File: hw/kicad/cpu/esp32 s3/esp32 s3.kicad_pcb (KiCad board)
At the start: 2 copper layers, 45 x 45 mm, 40 parts, among them J1 TOP, J2 BUTTOM, J3 USB_B_Micro, SW1 SW_Push, U1 ESP32-S3-WROOM-1-N16R2, U2 ICM-42688-P

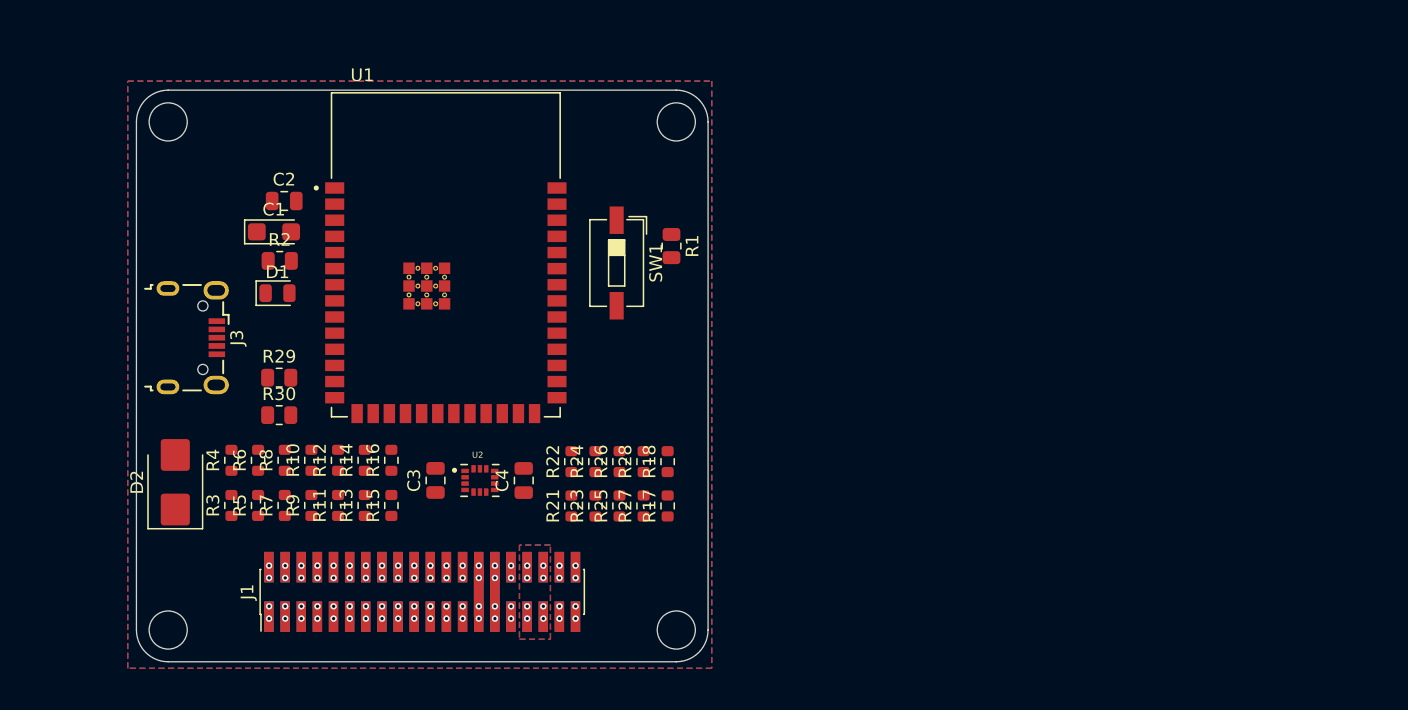
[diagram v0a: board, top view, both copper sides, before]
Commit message: 尽力改成40mmx40mm
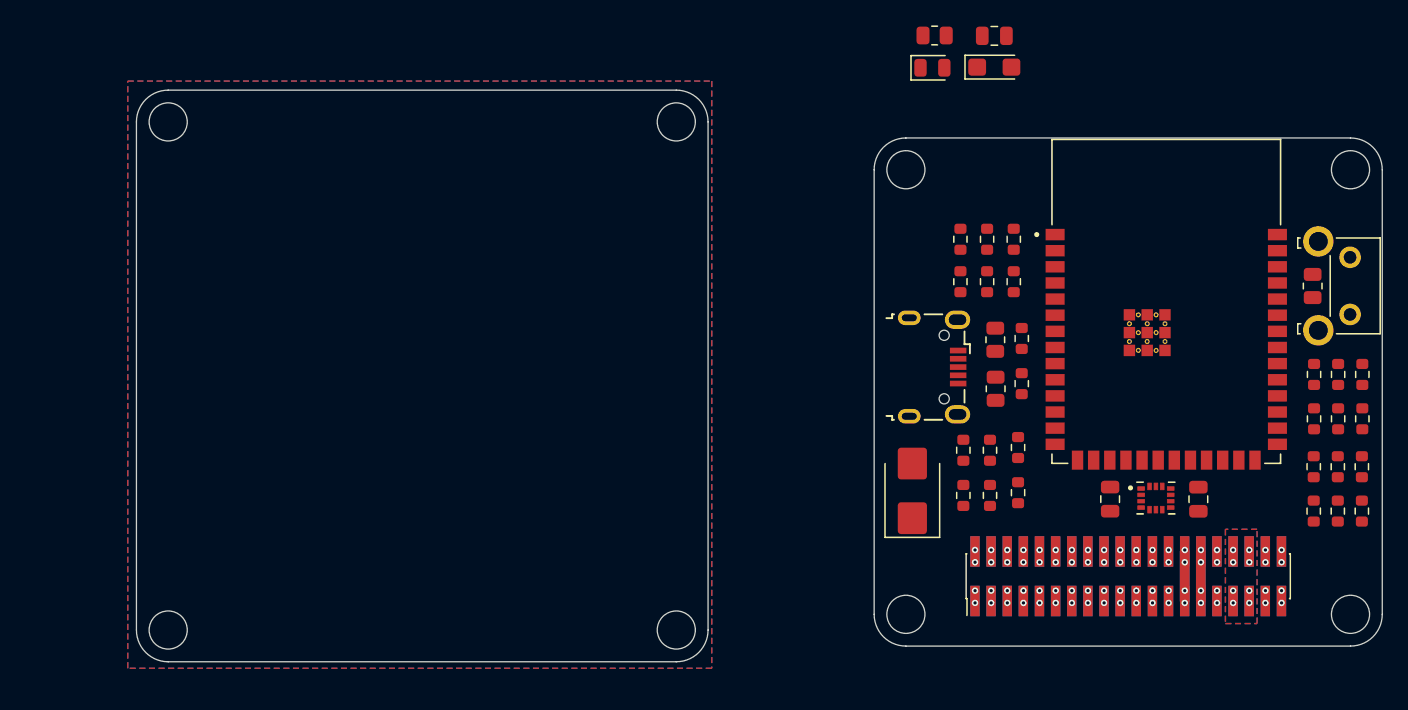
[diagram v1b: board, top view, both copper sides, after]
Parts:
- added R20: 100, Resistor_SMD:R_0603_1608Metric, F.Cu at (147.2, 58.6)
- added R31: 100, Resistor_SMD:R_0603_1608Metric, F.Cu at (147.2, 55.1)
- SW1: footprint Button_Switch_SMD:SW_DIP_SPSTx01_Slide_6.7x4.1mm_W6.73mm_P2.54mm_LowProfile_JPin -> Button_Switch_THT:SW_SPST_Omron_B3F-315x_Angled
- moved R3 60.0 mm to (115.6, 47.8)
- moved R5 60.0 mm to (117.7, 47.8)
- moved R7 60.0 mm to (119.8, 47.8)
- moved R4 60.0 mm to (115.6, 44.5)
- moved R6 60.0 mm to (117.7, 44.5)
- moved R8 60.0 mm to (119.8, 44.5)
- moved R25 58.4 mm to (147.2, 65.9)
- moved R21 58.4 mm to (143.4, 65.9)
- moved R23 58.4 mm to (145.3, 65.9)
- moved R26 58.4 mm to (147.2, 62.4)
- moved R22 58.4 mm to (143.4, 62.4)
- moved R24 58.4 mm to (145.3, 62.4)
- moved J3 58.4 mm to (113.5, 54.5)
- moved C1 58.2 mm to (118.3, 30.9)
- moved D2 58.0 mm to (111.8, 64.3)
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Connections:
- J1 pad 10: /UART3_Tx -> /I2C_CLK
- J1 pad 11: /I2C_SDA -> /SPI_CS
- J1 pad 12: /I2C_CLK -> /SPI_CLK
- J1 pad 13: /SPI_CS -> /SPI_MOSI
- J1 pad 14: /SPI_CLK -> /SPI_MISO
- J1 pad 15: /SPI_MOSI -> /GPIO_1
- J1 pad 16: /SPI_MISO -> /GPIO_2
- J1 pad 17: /GPIO_1 -> /GPIO_3
- J1 pad 18: /GPIO_2 -> /GPIO_4
- J1 pad 19: /GPIO_3 -> /GPIO_5
- J1 pad 20: /GPIO_4 -> /GPIO_6
- J1 pad 21: /GPIO_5 -> /GPIO_7
- J1 pad 22: /GPIO_6 -> /GPIO_8
- J1 pad 23: /GPIO_7 -> /GPIO_9
- J1 pad 24: /GPIO_8 -> /GPIO_10
- J1 pad 25: /GPIO_9 -> /GPIO_11
- J1 pad 26: /GPIO_10 -> /GPIO_12
- J1 pad 9: /UART3_Rx -> /I2C_SDA
- J2 pad 10: /UART3_Rx -> /I2C_SDA
- J2 pad 11: /I2C_CLK -> /SPI_CLK
- J2 pad 12: /I2C_SDA -> /SPI_CS
- J2 pad 13: /SPI_CLK -> /SPI_MISO
- J2 pad 14: /SPI_CS -> /SPI_MOSI
- J2 pad 15: /SPI_MISO -> /GPIO_2
- J2 pad 16: /SPI_MOSI -> /GPIO_1
- J2 pad 17: /GPIO_2 -> /GPIO_4
- J2 pad 18: /GPIO_1 -> /GPIO_3
- J2 pad 19: /GPIO_4 -> /GPIO_6
- J2 pad 20: /GPIO_3 -> /GPIO_5
- J2 pad 21: /GPIO_6 -> /GPIO_8
- J2 pad 22: /GPIO_5 -> /GPIO_7
- J2 pad 23: /GPIO_8 -> /GPIO_10
- J2 pad 24: /GPIO_7 -> /GPIO_9
- J2 pad 25: /GPIO_10 -> /GPIO_12
- J2 pad 26: /GPIO_9 -> /GPIO_11
- J2 pad 9: /UART3_Tx -> /I2C_CLK
- R10 pad 2: /UART2_TX -> /UART2_Tx
- R11 pad 1: /i2c_clk -> /i2c_sda
- R12 pad 1: /i2c_sda -> /i2c_clk
- R13 pad 1: /spi3_cs -> /spi2_cs
- R14 pad 1: /spi3_clk -> /spi2_clk
- R15 pad 1: /spi3_mosi -> /spi2_mosi
- R16 pad 1: /spi3_miso -> /spi2_miso
- R26 pad 1: /gpio5 -> /gpio6
- R29 pad 2: /USB+ -> /usb+
- R30 pad 2: /USB- -> /usb-
- R7 pad 2: /UART1_RX -> /UART1_Rx
- R8 pad 2: /UART1_TX -> /UART1_Tx
- R9 pad 2: /UART2_RX -> /UART2_Rx
- U1 pad 10: /i2c_clk -> /i2c_sda
- U1 pad 11: /i2c_sda -> /i2c_clk
- U1 pad 13: /usb_d- -> /usb-
- U1 pad 14: /usb_d+ -> /usb+
- U1 pad 15: unconnected-(U1-IO3-Pad15) -> /spi2_miso
- U1 pad 16: unconnected-(U1-IO46-Pad16) -> /spi2_cs
- U1 pad 17: /spi2_cs -> /spi2_mosi
- U1 pad 18: /spi2_mosi -> /spi2_clk
- U1 pad 19: /spi2_clk -> /spi3_miso
- U1 pad 20: /spi2_miso -> /IMU_FSYNC
- U1 pad 24: /spi3_miso -> /gpio1
- U1 pad 25: /IMU_FSYNC -> /gpio2
- U1 pad 26: unconnected-(U1-IO45-Pad26) -> Net-(U1-IO45)
- U1 pad 28: /gpio1 -> /gpio3
- U1 pad 29: /gpio2 -> /gpio4
- U1 pad 30: /gpio3 -> /gpio5
- U1 pad 31: /gpio4 -> /gpio6
- U1 pad 32: /gpio5 -> /gpio7
- U1 pad 33: /gpio5 -> /gpio8
- U1 pad 34: /gpio7 -> /gpio9
- U1 pad 35: /gpio8 -> /gpio10
- U1 pad 38: /gpio9 -> /gpio11
- U1 pad 39: /gpio10 -> /gpio12
- U1 pad 8: /uart1_tx -> /uart1_rx
- U1 pad 9: /uart1_rx -> /uart1_tx
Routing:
- net /UART3_Tx: vias 2 -> 0
- net /UART3_Rx: vias 2 -> 0
- net /GPIO_12: vias 0 -> 2
- net /GPIO_11: vias 0 -> 2
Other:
- board size 45 x 45 mm -> 98.1 x 45 mm

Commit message: esp32部分该小板框可太难了，小电阻太多，只好全部去掉。
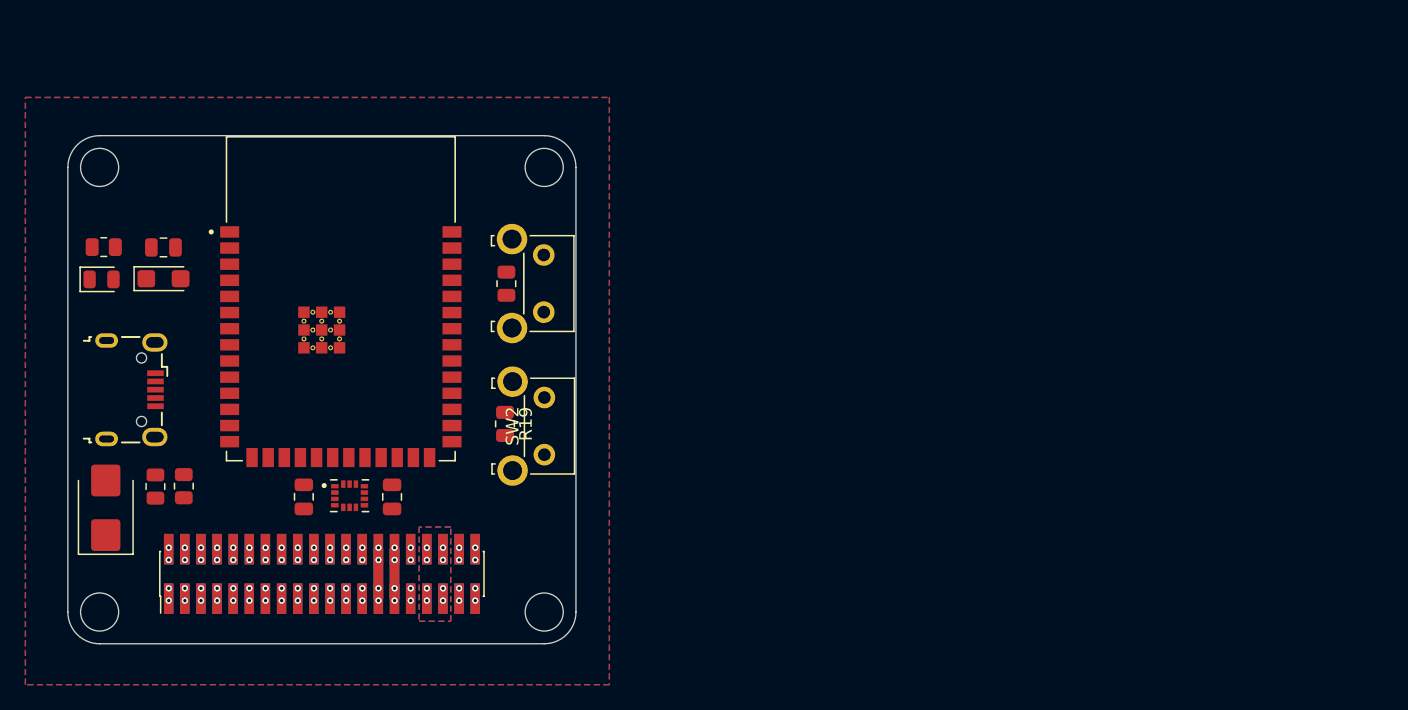
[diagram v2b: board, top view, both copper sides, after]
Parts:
- removed R10, R11, R12, R13, R14, R15, R16, R17, R18, R20, R21, R22, R23, R24, R25, R26, R27, R28, R3, R31, R4, R5, R6, R7, R8, R9: 100, Resistor_SMD:R_0603_1608Metric
- added R19: 1k, Resistor_SMD:R_0805_2012Metric, F.Cu at (79.7, 59.0)
- added SW2: SW_Push, Button_Switch_THT:SW_SPST_Omron_B3F-315x_Angled, F.Cu at (82.8, 56.9)
- moved C1 67.5 mm to (52.8, 47.6)
- moved C2 67.5 mm to (52.8, 45.1)
- moved D1 67.5 mm to (48.0, 47.6)
- moved R2 67.5 mm to (48.1, 45.1)
- moved R30 67.1 mm to (52.2, 63.9)
- moved U1 65.0 mm to (66.8, 49.1)
- moved R29 64.4 mm to (54.5, 63.9)
- moved D2 63.5 mm to (48.3, 65.6)
- moved R1 63.5 mm to (79.8, 48.0)
- moved U2 63.5 mm to (67.5, 64.6)
- moved C3 63.5 mm to (63.9, 64.7)
- moved C4 63.5 mm to (70.8, 64.7)
- moved SW1 63.5 mm to (82.8, 45.7)
- moved J1 63.5 mm to (65.3, 70.8)
- moved J2 63.5 mm to (65.3, 70.8)
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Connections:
- U1 pad 10: /i2c_sda -> /I2C_SDA
- U1 pad 11: /i2c_clk -> /I2C_CLK
- U1 pad 15: /spi2_miso -> /SPI_MISO
- U1 pad 16: /spi2_cs -> /SPI_CS
- U1 pad 17: /spi2_mosi -> /SPI_MOSI
- U1 pad 18: /spi2_clk -> /SPI_CLK
- U1 pad 24: /gpio1 -> /GPIO_1
- U1 pad 25: /gpio2 -> /GPIO_2
- U1 pad 28: /gpio3 -> /GPIO_3
- U1 pad 29: /gpio4 -> /GPIO_4
- U1 pad 30: /gpio5 -> /GPIO_5
- U1 pad 31: /gpio6 -> /GPIO_6
- U1 pad 32: /gpio7 -> /GPIO_7
- U1 pad 33: /gpio8 -> /GPIO_8
- U1 pad 34: /gpio9 -> /GPIO_9
- U1 pad 35: /gpio10 -> /GPIO_10
- U1 pad 36: /uart0_rx -> /UART1_Rx
- U1 pad 37: /uart0_tx -> /UART1_Tx
- U1 pad 38: /gpio11 -> /GPIO_11
- U1 pad 39: /gpio12 -> /GPIO_12
- U1 pad 4: /adc1_ch3 -> /ADC_1
- U1 pad 5: /adc1_ch4 -> /ADC_2
- U1 pad 6: /adc1_ch5 -> /ADC_3
- U1 pad 7: /adc1_ch6 -> /ADC_4
- U1 pad 8: /uart1_rx -> /UART2_Rx
- U1 pad 9: /uart1_tx -> /UART2_Tx
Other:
- board size 98.1 x 45 mm -> 40 x 40 mm

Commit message: Merge from normal
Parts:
- removed SW2: SW_Push, Button_Switch_THT:SW_SPST_Omron_B3F-315x_Angled
- added R10: R, Resistor_SMD:R_0603_1608Metric, F.Cu at (65.4, 52.3)
- added R11: R, Resistor_SMD:R_0603_1608Metric, F.Cu at (65.4, 53.8)
- added R12: R, Resistor_SMD:R_0603_1608Metric, F.Cu at (65.4, 55.3)
- added R13: R, Resistor_SMD:R_0603_1608Metric, F.Cu at (65.4, 56.8)
- added R14: R, Resistor_SMD:R_0603_1608Metric, F.Cu at (65.4, 58.3)
- added R15: R, Resistor_SMD:R_0603_1608Metric, F.Cu at (65.4, 59.8)
- added R16: R, Resistor_SMD:R_0603_1608Metric, F.Cu at (65.4, 61.3)
- added R17: R, Resistor_SMD:R_0603_1608Metric, F.Cu at (90.2, 58.4)
- added R18: R, Resistor_SMD:R_0603_1608Metric, F.Cu at (90.2, 56.9)
- added R20: R, Resistor_SMD:R_0603_1608Metric, F.Cu at (90.2, 53.8)
- added R21: R, Resistor_SMD:R_0603_1608Metric, F.Cu at (90.2, 52.3)
- added R22: R, Resistor_SMD:R_0603_1608Metric, F.Cu at (90.2, 50.8)
- added R23: R, Resistor_SMD:R_0603_1608Metric, F.Cu at (90.2, 49.3)
- added R24: R, Resistor_SMD:R_0603_1608Metric, F.Cu at (90.2, 47.8)
- added R25: R, Resistor_SMD:R_0603_1608Metric, F.Cu at (90.2, 46.3)
- added R26: R, Resistor_SMD:R_0603_1608Metric, F.Cu at (90.2, 44.8)
- added R27: R, Resistor_SMD:R_0603_1608Metric, F.Cu at (90.2, 43.3)
- added R28: R, Resistor_SMD:R_0603_1608Metric, F.Cu at (90.2, 41.7)
- added R3: R, Resistor_SMD:R_0603_1608Metric, F.Cu at (65.4, 41.8)
- added R4: R, Resistor_SMD:R_0603_1608Metric, F.Cu at (65.4, 43.3)
- added R5: R, Resistor_SMD:R_0603_1608Metric, F.Cu at (65.4, 44.8)
- added R6: R, Resistor_SMD:R_0603_1608Metric, F.Cu at (65.4, 46.3)
- added R7: R, Resistor_SMD:R_0603_1608Metric, F.Cu at (65.4, 47.8)
- added R8: R, Resistor_SMD:R_0603_1608Metric, F.Cu at (65.4, 49.3)
- added R9: R, Resistor_SMD:R_0603_1608Metric, F.Cu at (65.4, 50.8)
- R1: footprint Resistor_SMD:R_0805_2012Metric -> Resistor_SMD:R_0603_1608Metric
- R19: value 1k -> R; footprint Resistor_SMD:R_0805_2012Metric -> Resistor_SMD:R_0603_1608Metric
- R29, R30: footprint Resistor_SMD:R_0805_2012Metric -> Resistor_SMD:R_0603_1608Metric; moved to B.Cu
- moved R2 49.6 mm to (89.7, 72.2)
- moved D1 47.4 mm to (89.7, 70.2), turned to 180 degrees
- moved SW1 30.0 mm to (53.4, 51.3), turned to 90 degrees
- moved R1 22.1 mm to (57.8, 49.0)
- moved R30 15.6 mm to (65.4, 55.7), turned to 0 degrees
- moved R29 12.7 mm to (65.4, 57.4), turned to 0 degrees
- moved U1 11.6 mm to (77.9, 45.7)
- moved C3 11.5 mm to (75.2, 62.4)
- moved C4 11.5 mm to (82.1, 62.4)
- moved U2 11.4 mm to (78.7, 62.4)
- moved R19 11.1 mm to (90.2, 55.4), turned to 0 degrees
- moved C2 8.58 mm to (60.6, 41.4), turned to -90 degrees
- moved J1 8.02 mm to (73.2, 72.2)
- moved J2 8.02 mm to (73.2, 72.2)
- moved C1 7.78 mm to (58.2, 42.0), turned to -90 degrees
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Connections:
- R1 pad 1: GND -> Net-(R1-Pad1)
- R1 pad 2: Net-(R1-Pad2) -> Net-(U1-IO0)
- R19 pad 1: GND -> /gpio3
- R19 pad 2: Net-(R19-Pad2) -> /GPIO_3
- SW1 pad 1: Net-(R1-Pad2) -> GND
- SW1 pad 2: Net-(U1-IO0) -> Net-(R1-Pad1)
- U1 pad 10: /I2C_SDA -> /i2c_sda
- U1 pad 11: /I2C_CLK -> /i2c_clk
- U1 pad 12: /LED -> unconnected-(U1-IO8-Pad12)
- U1 pad 15: /SPI_MISO -> /spi3_cs
- U1 pad 16: /SPI_CS -> /spi3_clk
- U1 pad 17: /SPI_MOSI -> /spi3_mosi
- U1 pad 18: /SPI_CLK -> /spi3_miso
- U1 pad 19: /spi3_miso -> /spi2_miso
- U1 pad 20: /IMU_FSYNC -> /spi2_mosi
- U1 pad 21: /spi3_cs -> /spi2_clk
- U1 pad 22: /spi3_clk -> /spi2_cs
- U1 pad 23: /spi3_mosi -> /IMU_FSYNC
- U1 pad 24: /GPIO_1 -> /LED
- U1 pad 25: /GPIO_2 -> /gpio1
- U1 pad 26: Net-(U1-IO45) -> /gpio2
- U1 pad 28: /GPIO_3 -> /gpio3
- U1 pad 29: /GPIO_4 -> /gpio4
- U1 pad 30: /GPIO_5 -> /gpio5
- U1 pad 31: /GPIO_6 -> /gpio6
- U1 pad 32: /GPIO_7 -> /gpio7
- U1 pad 33: /GPIO_8 -> /gpio8
- U1 pad 34: /GPIO_9 -> /gpio9
- U1 pad 35: /GPIO_10 -> /gpio10
- U1 pad 36: /UART1_Rx -> /uart0_rx
- U1 pad 37: /UART1_Tx -> /uart0_tx
- U1 pad 38: /GPIO_11 -> /gpio11
- U1 pad 39: /GPIO_12 -> /gpio12
- U1 pad 4: /ADC_1 -> /adc1_ch3
- U1 pad 41_10: (no net) -> GND
- U1 pad 41_11: (no net) -> GND
- U1 pad 41_12: (no net) -> GND
- U1 pad 41_13: (no net) -> GND
- U1 pad 41_14: (no net) -> GND
- U1 pad 41_15: (no net) -> GND
- U1 pad 41_16: (no net) -> GND
- U1 pad 41_17: (no net) -> GND
- U1 pad 41_18: (no net) -> GND
- U1 pad 41_19: (no net) -> GND
- U1 pad 41_20: (no net) -> GND
- U1 pad 41_21: (no net) -> GND
- U1 pad 5: /ADC_2 -> /adc1_ch4
- U1 pad 6: /ADC_3 -> /adc1_ch5
- U1 pad 7: /ADC_4 -> /adc1_ch6
- U1 pad 8: /UART2_Rx -> /uart1_rx
- U1 pad 9: /UART2_Tx -> /uart1_tx
- U2 pad 1: /spi3_miso -> /spi2_miso
- U2 pad 12: /spi3_cs -> /spi2_cs
- U2 pad 13: /spi3_clk -> /spi2_clk
- U2 pad 14: /spi3_mosi -> /spi2_mosi
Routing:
- net +3.3V: track 7.80 -> 72.4 mm, vias 4 -> 6
- net /GPIO_11: track 0.00 -> 50.7 mm
- net /GPIO_12: track 0.00 -> 48.7 mm
- net /GPIO_9: track 0.00 -> 48.3 mm
- net /GPIO_10: track 0.00 -> 45.7 mm
- net /GPIO_7: track 0.00 -> 45.0 mm
- net /GPIO_8: track 0.00 -> 42.5 mm
- net /GPIO_5: track 0.00 -> 41.7 mm
- net /GPIO_6: track 0.00 -> 39.3 mm
- net /GPIO_3: track 0.00 -> 38.3 mm
- net /ADC_1: track 0.00 -> 36.3 mm
- net /GPIO_4: track 0.00 -> 35.8 mm
- net /GPIO_1: track 0.00 -> 35.0 mm
- net /ADC_3: track 0.00 -> 33.7 mm, vias 2 -> 1
- net /GPIO_2: track 0.00 -> 32.7 mm
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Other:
- board size 40 x 40 mm -> 45 x 45 mm
- board text added: "Pindar v1.2 (CPU) ESP32 S3 v1.2"

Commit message: 更新打样资料
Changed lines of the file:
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@@
     (fp_line (start 1 0.625) (end -1 0.625)
       (stroke (width 0.1) (type solid)) (layer "F.Fab"))
-    (pad "1" smd roundrect (at -0.9125 0) (size 1.025 1.4) (layers "F.Cu" "F.Paste" "F.Mask") (roundrect_rratio 0.243902)
+    (pad "1" smd roundrect (at -0.9125 0) (size 1.025 1.4) (layers "F.Cu" "F.Paste" "F.Mask") (roundrect_rratio 0.243902439)
       (net 26 "GND") (pintype "passive"))
-    (pad "2" smd roundrect (at 0.9125 0) (size 1.025 1.4) (layers "F.Cu" "F.Paste" "F.Mask") (roundrect_rratio 0.243902)
+    (pad "2" smd roundrect (at 0.9125 0) (size 1.025 1.4) (layers "F.Cu" "F.Paste" "F.Mask") (roundrect_rratio 0.243902439)
       (net 29 "Net-(D1-K)") (pintype "passive"))
     (model "${KICAD6_3DMODEL_DIR}/Resistor_SMD.3dshapes/R_0805_2012Metric.wrl"
@@
     (fp_line (start 1.6 0.8) (end 1.6 -0.8)
       (stroke (width 0.1) (type solid)) (layer "F.Fab"))
-    (pad "1" smd roundrect (at -1.35 0 270) (size 1.4 1.35) (layers "F.Cu" "F.Paste" "F.Mask") (roundrect_rratio 0.185185)
+    (pad "1" smd roundrect (at -1.35 0 270) (size 1.4 1.35) (layers "F.Cu" "F.Paste" "F.Mask") (roundrect_rratio 0.1851851852)
       (net 1 "+3.3V") (pintype "passive"))
-    (pad "2" smd roundrect (at 1.35 0 270) (size 1.4 1.35) (layers "F.Cu" "F.Paste" "F.Mask") (roundrect_rratio 0.185185)
+    (pad "2" smd roundrect (at 1.35 0 270) (size 1.4 1.35) (layers "F.Cu" "F.Paste" "F.Mask") (roundrect_rratio 0.1851851852)
       (net 26 "GND") (pintype "passive"))
     (model "${KICAD6_3DMODEL_DIR}/Capacitor_Tantalum_SMD.3dshapes/CP_EIA-3216-12_Kemet-S.wrl"
@@
   (via (at 69.1458 65.6188) (size 0.762) (drill 0.381) (layers "F.Cu" "B.Cu") (free) (net 26))
   (via (at 82.6332 41.6158) (size 0.762) (drill 0.381) (layers "F.Cu" "B.Cu") (free) (net 26))
-  (via (at 80.1694 60.6404) (size 0.762) (drill 0.381) (layers "F.Cu" "B.Cu") (free) (net 26))
+  (via (at 80.3472 59.5736) (size 0.762) (drill 0.381) (layers "F.Cu" "B.Cu") (free) (net 26))
   (via (at 84.0232 71.12) (size 0.508) (drill 0.254) (layers "F.Cu" "B.Cu") (net 26))
   (via (at 80.2132 70.1548) (size 0.508) (drill 0.254) (layers "F.Cu" "B.Cu") (net 26))
